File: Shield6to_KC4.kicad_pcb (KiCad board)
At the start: 2 copper layers, 112.4 x 80 mm, 33 parts, among them J1 DB9, P1 CONN_9, P2 CONN_8, P3 CONN_9, P4 CONN_8, P5 CONN_8, P8 CONN_8, SW1 BOOT/BOT1, SW2 BOT2, SW3 BOT3, SW4 BOT4, SW5 RESET, U1 ID-12LA, U2 MAX232

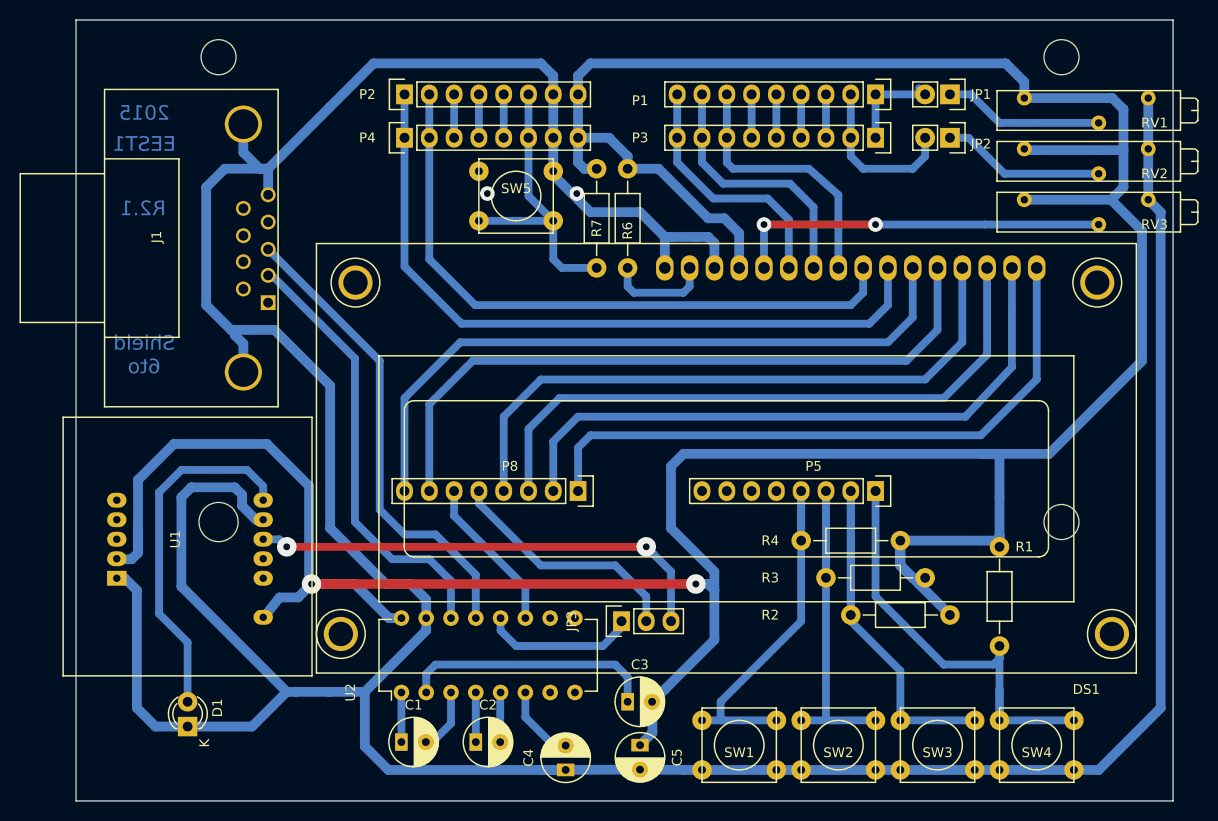
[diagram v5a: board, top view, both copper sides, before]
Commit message: Changes to be committed: 	modified:   Modelodelgabinete.fcstd 	modified:   Modelodelgabinete.fcstd1 	new file:   Modelodelgabinete3.fcstd 	new file:   Modelodelgabinete4.fcstd 	new file:   Modelodelgabinete4.fcstd1 	new file:   Modelodelgabinete5.fcstd 	new file:   Modelodelgabinete5.fcstd1 	new file:   ProbandoFreecad17.fcstd 	new file:   ProbandoFreecad17.fcstd1 	modified:   Shield6to_KC4-cache.lib 	modified:   Shield6to_KC4.bak 	modified:   Shield6to_KC4.kicad_pcb 	modified:   Shield6to_KC4.kicad_pcb-bak 	modified:   Shield6to_KC4.sch 	new file:   box2.stl 	new file:   box3.pro 	new file:   box3.stl 	new file:   box_Rev1.stl
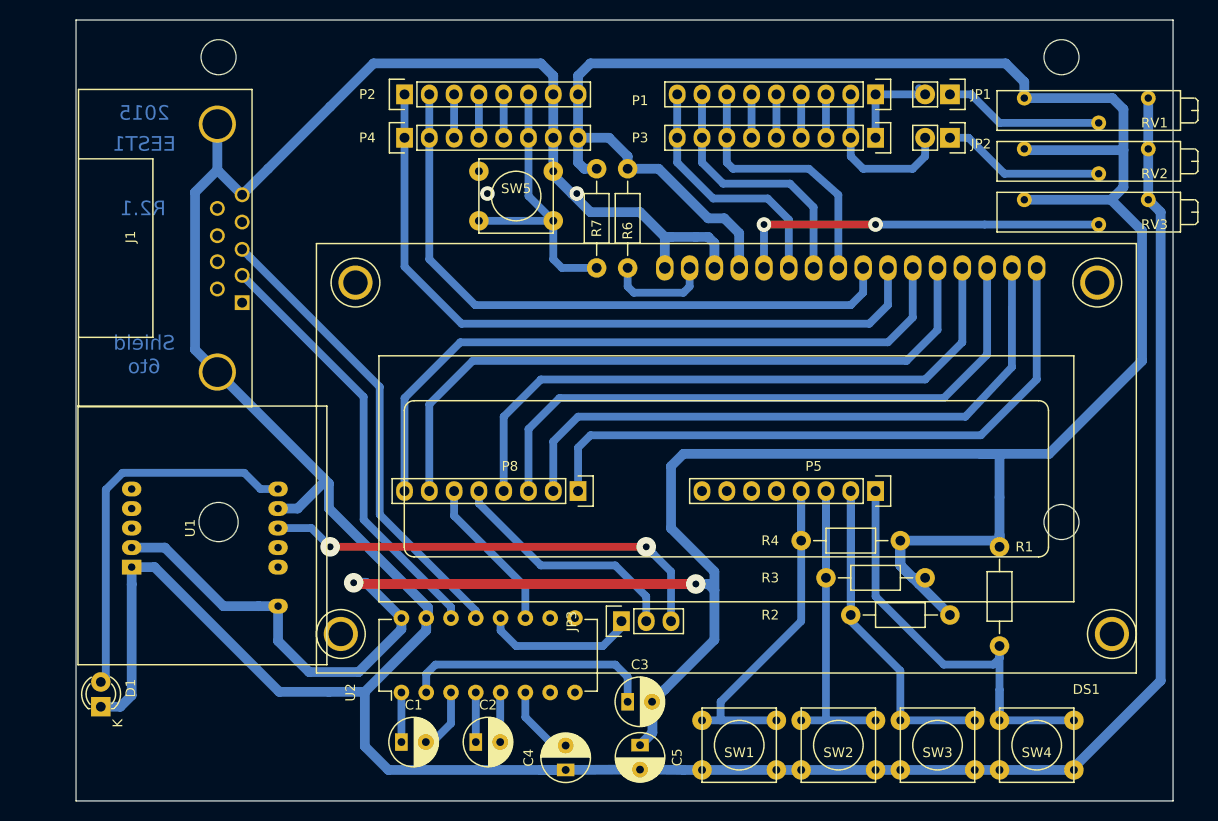
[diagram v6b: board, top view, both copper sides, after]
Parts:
- moved D1 9.12 mm to (57.8, 123.7)
- moved J1 2.67 mm to (71.0, 76.8)
- moved U1 1.90 mm to (67.9, 104.4)
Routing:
- net GND: track 391.4 -> 357.4 mm
- net +5V: track 369.8 -> 349.2 mm
- net Net-(D1-Pad2): track 36.4 -> 39.0 mm
- net Net-(J1-Pad2): track 45.3 -> 44.0 mm
- net Tarjeta: track 48.2 -> 47.2 mm
- net Net-(J1-Pad3): track 48.5 -> 47.7 mm
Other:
- net class Default: clearance 0.2 -> 0.5
- net class Power: clearance 0.2 -> 0.5
- rule trace_clearance: 0.2 -> 0.5
